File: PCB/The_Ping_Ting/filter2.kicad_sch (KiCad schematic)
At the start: 18 parts, among them SW301 SW_SP3T, U105 LM324

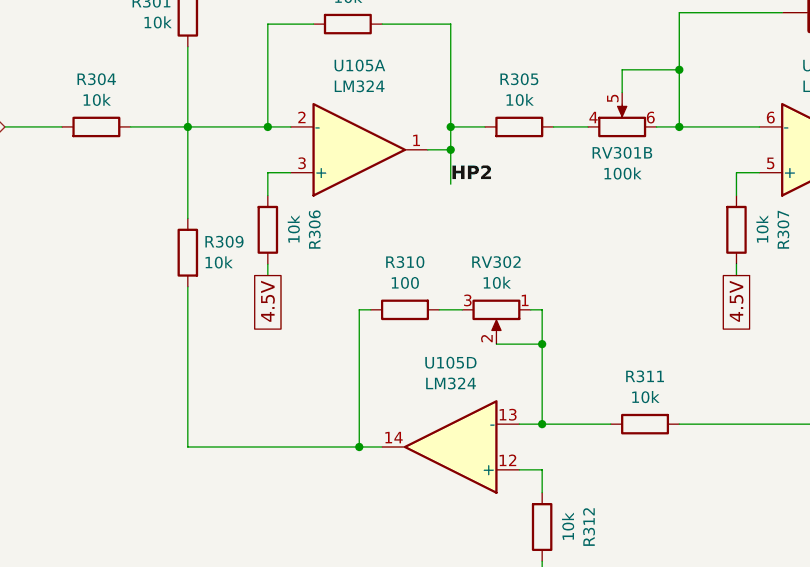
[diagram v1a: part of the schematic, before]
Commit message: REVV 1.2 - Updated resonance feedback resistance Updated the feedback resistance in the mid and high frequency feedback circuit to get a more "stable" resonance level.
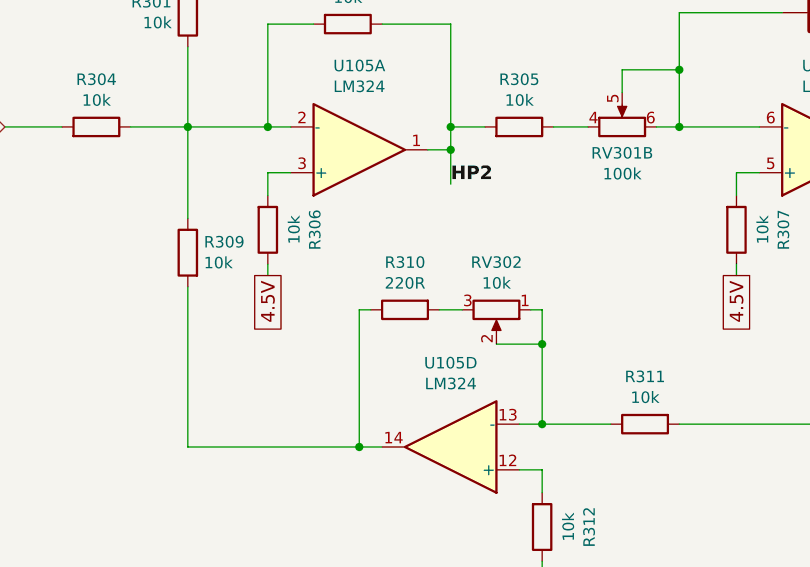
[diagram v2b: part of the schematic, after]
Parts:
- R310: value 100 -> 220R
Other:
- company: (none) -> Kromftronics
- title: (none) -> Mid Frequency Filter
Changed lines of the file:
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@@
 	(generator_version "8.0")
 	(paper "A4")
+	(title_block
+		(title "Mid Frequency Filter")
+		(date "2024-09-07")
+		(rev "1.2")
+		(company "Kromftronics")
+	)
 	(junction
 		(at 90.17 93.98)
@@
 			)
 		)
-		(property "Value" "100"
+		(property "Value" "220R"
 			(at 114.3 111.3536 90)
 			(effects
